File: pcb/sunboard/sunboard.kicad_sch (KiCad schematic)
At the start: 155 parts, among them SW1 SW_Push, SW10 SW_Push, SW100 SW_Push, SW101 SW_Push, SW102 SW_Push, SW103 SW_Push, SW104 SW_Push, SW105 SW_Push, SW106 SW_Push, SW107 SW_Push, SW108 SW_Push, SW109 SW_Push, SW11 SW_Push, SW110 SW_Push, SW111 SW_Push, SW112 SW_Push, SW113 SW_Push, SW114 SW_Push, SW115 SW_Push, SW116 SW_Push, SW117 SW_Push, SW118 SW_Push, SW119 SW_Push, SW12 SW_Push, SW120 SW_Push, SW121 SW_Push, SW122 SW_Push, SW123 SW_Push, SW124 SW_Push, SW125 SW_Push, SW126 SW_Push, SW127 SW_Push, SW128 SW_Push, SW129 SW_Push, SW13 SW_Push, SW130 SW_Push, SW131 SW_Push, SW132 SW_Push, SW133 SW_Push, SW134 SW_Push, SW135 SW_Push, SW136 SW_Push, SW137 SW_Push, SW138 SW_Push, SW139 SW_Push, SW14 SW_Push, SW140 SW_Push, SW141 SW_Push, SW142 SW_Push, SW143 SW_Push, SW144 SW_Push, SW145 SW_Push, SW146 SW_Push, SW147 SW_Push, SW148 SW_Push, SW149 SW_Push, SW15 SW_Push, SW150 SW_Push, SW151 SW_Push, SW152 SW_Push, SW153 SW_Push, SW154 SW_Push, SW16 SW_Push, SW17 SW_Push, SW18 SW_Push, SW19 SW_Push, SW2 SW_Push, SW20 SW_Push, SW21 SW_Push, SW22 SW_Push, SW23 SW_Push, SW24 SW_Push, SW25 SW_Push, SW26 SW_Push, SW27 SW_Push, SW28 SW_Push, SW29 SW_Push, SW3 SW_Push, SW30 SW_Push, SW31 SW_Push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

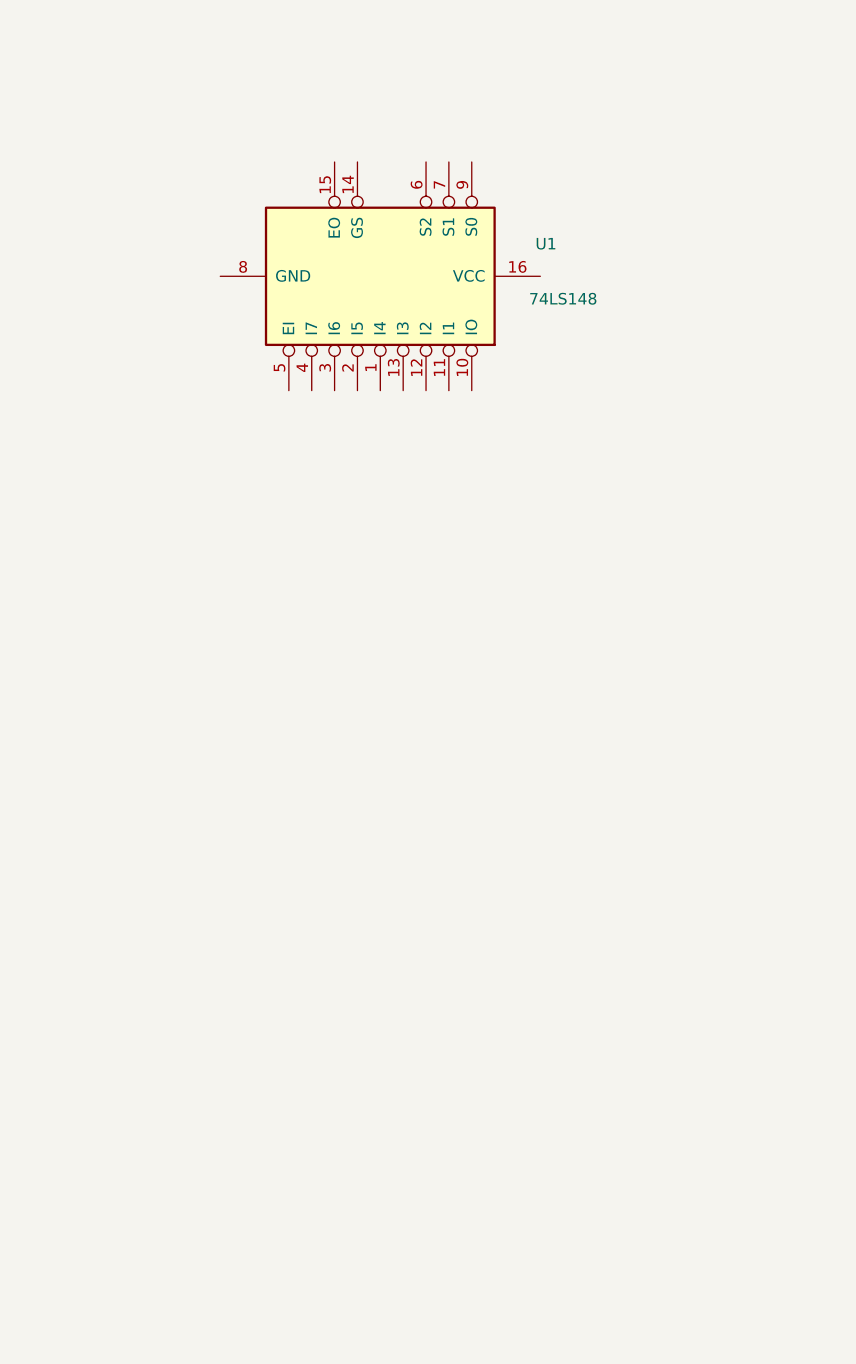
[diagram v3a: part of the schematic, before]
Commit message: feat(pcb): add 74hc4067 for mux/demux
Now the board uses 74hc4067 for both mux / demux purposes. A surprisingly nice chip with both functionalities. Might use it for the lights also
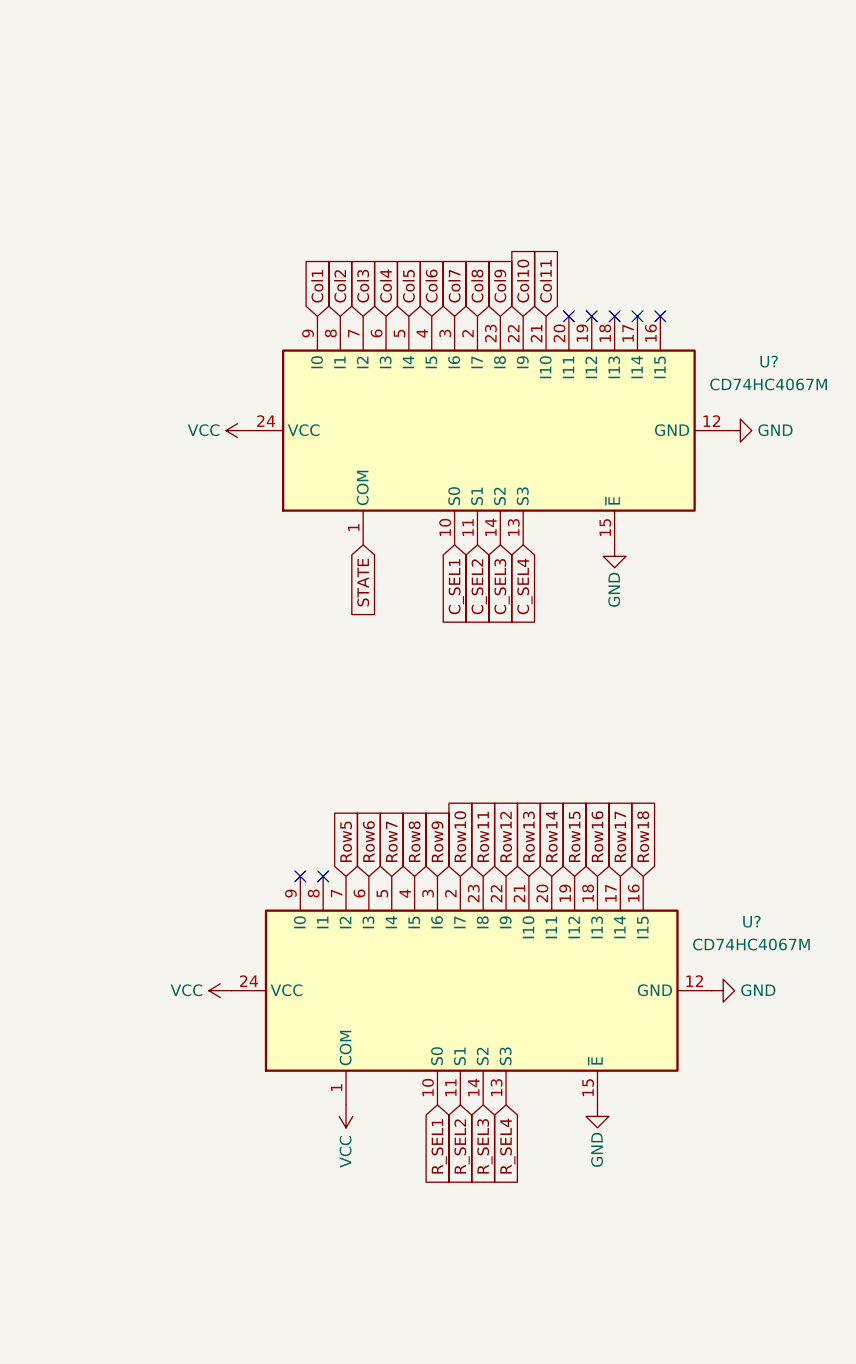
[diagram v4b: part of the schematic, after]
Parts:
- removed U1: 74LS148, symbol 74xx:74LS148
- added U? (x2): CD74HC4067M, Package_SO:SOIC-24W_7.5x15.4mm_P1.27mm, symbol 74xx:CD74HC4067M
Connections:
- net Col1: now also U?.9 (I0)
- net Col10: now also U?.22 (I9)
- net Col11: now also U?.21 (I10)
- net Col2: now also U?.8 (I1)
- net Col3: now also U?.7 (I2)
- net Col4: now also U?.6 (I3)
- net Col5: now also U?.5 (I4)
- net Col6: now also U?.4 (I5)
- net Col7: now also U?.3 (I6)
- net Col8: now also U?.2 (I7)
- net Col9: now also U?.23 (I8)
- net Row10: now also U?.2 (I7)
- net Row11: now also U?.23 (I8)
- net Row12: now also U?.22 (I9)
- net Row13: now also U?.21 (I10)
- net Row14: now also U?.20 (I11)
- net Row15: now also U?.19 (I12)
- net Row16: now also U?.18 (I13)
- net Row17: now also U?.17 (I14)
- net Row18: now also U?.16 (I15)
- net Row5: now also U?.7 (I2)
- net Row6: now also U?.6 (I3)
- net Row7: now also U?.5 (I4)
- net Row8: now also U?.4 (I5)
- net Row9: now also U?.3 (I6)
- new net C_SEL1: U?.10 (S0)
- new net C_SEL2: U?.11 (S1)
- new net C_SEL3: U?.14 (S2)
- new net C_SEL4: U?.13 (S3)
- new net GND: U?.12 (GND), U?.12 (GND), U?.15 (~{E}), U?.15 (~{E})
- new net R_SEL1: U?.10 (S0)
- new net R_SEL2: U?.11 (S1)
- new net R_SEL3: U?.14 (S2)
- new net R_SEL4: U?.13 (S3)
- new net STATE: U?.1 (COM)
- new net VCC: U?.1 (COM), U?.24 (VCC), U?.24 (VCC)
- no-connect marks 0 -> 7

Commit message: feat(pcb): migrate to subsheets
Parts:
- removed SW1, SW10, SW100, SW101, SW102, SW103, SW104, SW105, SW106, SW107, SW108, SW109, SW11, SW110, SW111, SW112, SW113, SW114, SW115, SW116, SW117, SW118, SW119, SW12, SW120, SW121, SW122, SW123, SW124, SW125, SW126, SW127, SW128, SW129, SW13, SW130, SW131, SW132, SW133, SW134, SW135, SW136, SW137, SW138, SW139, SW14, SW140, SW141, SW142, SW143, SW144, SW145, SW146, SW147, SW148, SW149, SW15, SW150, SW151, SW152, SW153, SW154, SW16, SW17, SW18, SW19, SW2, SW20, SW21, SW22, SW23, SW24, SW25, SW26, SW27, SW28, SW29, SW3, SW30, SW31, SW32, SW33, SW34, SW35, SW36, SW37, SW38, SW39, SW4, SW40, SW41, SW42, SW43, SW44, SW45, SW46, SW47, SW48, SW49, SW5, SW50, SW51, SW52, SW53, SW54, SW55, SW56, SW57, SW58, SW59, SW6, SW60, SW61, SW62, SW63, SW64, SW65, SW66, SW67, SW68, SW69, SW7, SW70, SW71, SW72, SW73, SW74, SW75, SW76, SW77, SW78, SW79, SW8, SW80, SW81, SW82, SW83, SW84, SW85, SW86, SW87, SW88, SW89, SW9, SW90, SW91, SW92, SW93, SW94, SW95, SW96, SW97, SW98, SW99: SW_Push, symbol Switch:SW_Push
- added U3: ESP32_NODEMCU, ESP32_NODEMCU:MODULE_ESP32_NODEMCU, symbol ESP32_NODEMCU:ESP32_NODEMCU
- gave numbers to parts that had none: 2
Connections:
- net GND: now also U3.J4_1 (GND_J4_1), U3.J4_7 (GND_J4_7), U3.J5_6 (GND_J5_6)
- net VCC: now also U3.J5_1 (5V)
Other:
- added sheet Button_Matrix (Button_Matrix.kicad_sch)
- added sheet LED_Matrix (LED_Matrix.kicad_sch)
- moved on the sheet: U1, U2

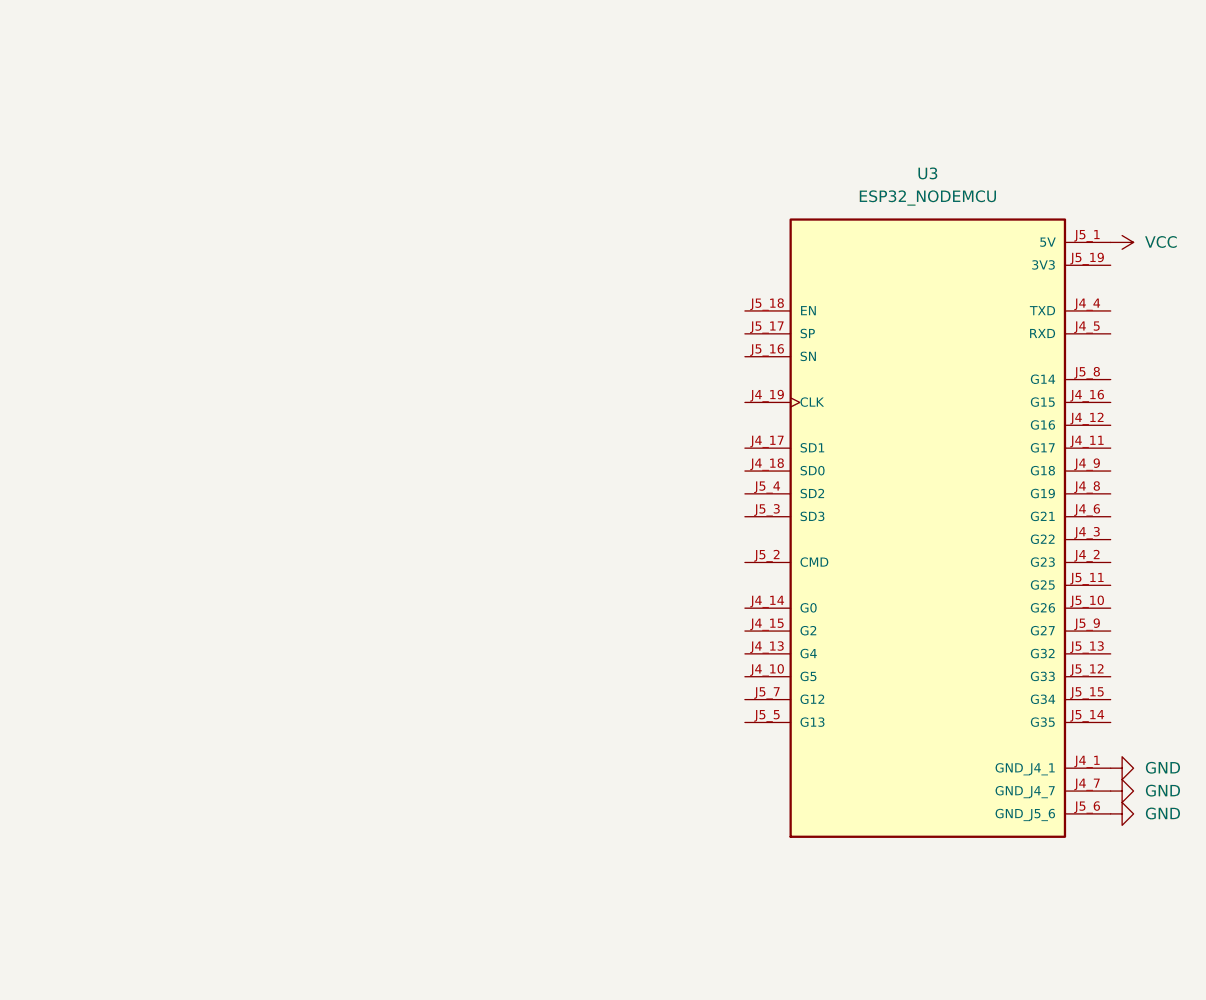
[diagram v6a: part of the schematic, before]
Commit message: feat(pcb): remove led driver, layout main grid
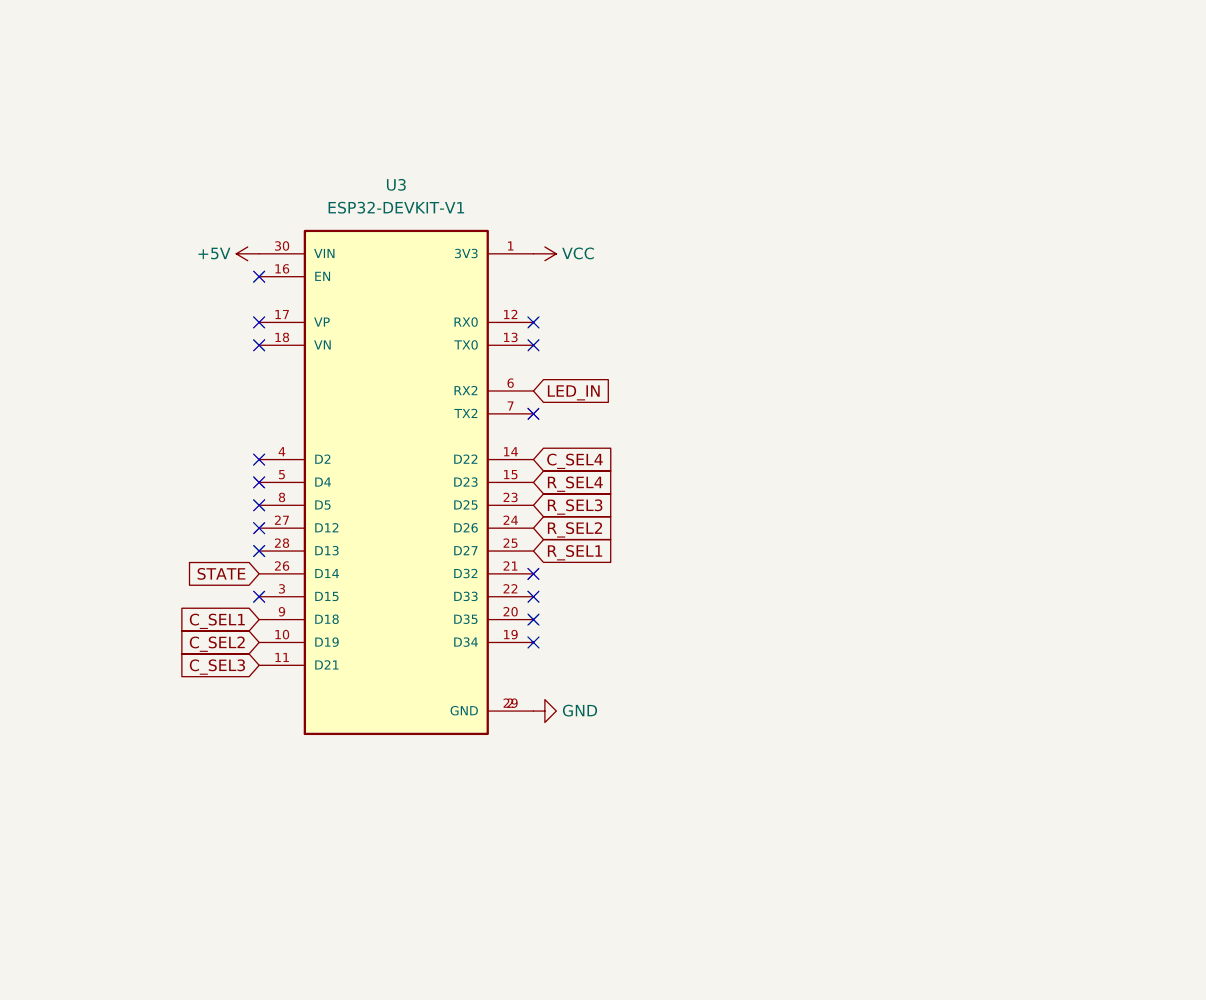
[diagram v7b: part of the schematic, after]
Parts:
- removed U3: ESP32_NODEMCU, ESP32_NODEMCU:MODULE_ESP32_NODEMCU, symbol ESP32_NODEMCU:ESP32_NODEMCU
- added U3: ESP32-DEVKIT-V1, ESP32-DEVKIT-V1:MODULE_ESP32_DEVKIT_V1, symbol ESP32-DEVKIT-V1:ESP32-DEVKIT-V1
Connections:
- net C_SEL1: now also U3.9 (D18)
- net C_SEL2: now also U3.10 (D19)
- net C_SEL3: now also U3.11 (D21)
- net C_SEL4: now also U3.14 (D22)
- net GND: now also U3.2 (GND), U3.29 (GND)
- net R_SEL1: now also U3.25 (D27)
- net R_SEL2: now also U3.24 (D26)
- net R_SEL3: now also U3.23 (D25)
- net R_SEL4: now also U3.15 (D23)
- net STATE: now also U3.26 (D14)
- net VCC: now also U3.1 (3V3)
- new net +5V: U3.30 (VIN)
- new net LED_IN: U3.6 (RX2)
- no-connect marks 7 -> 23

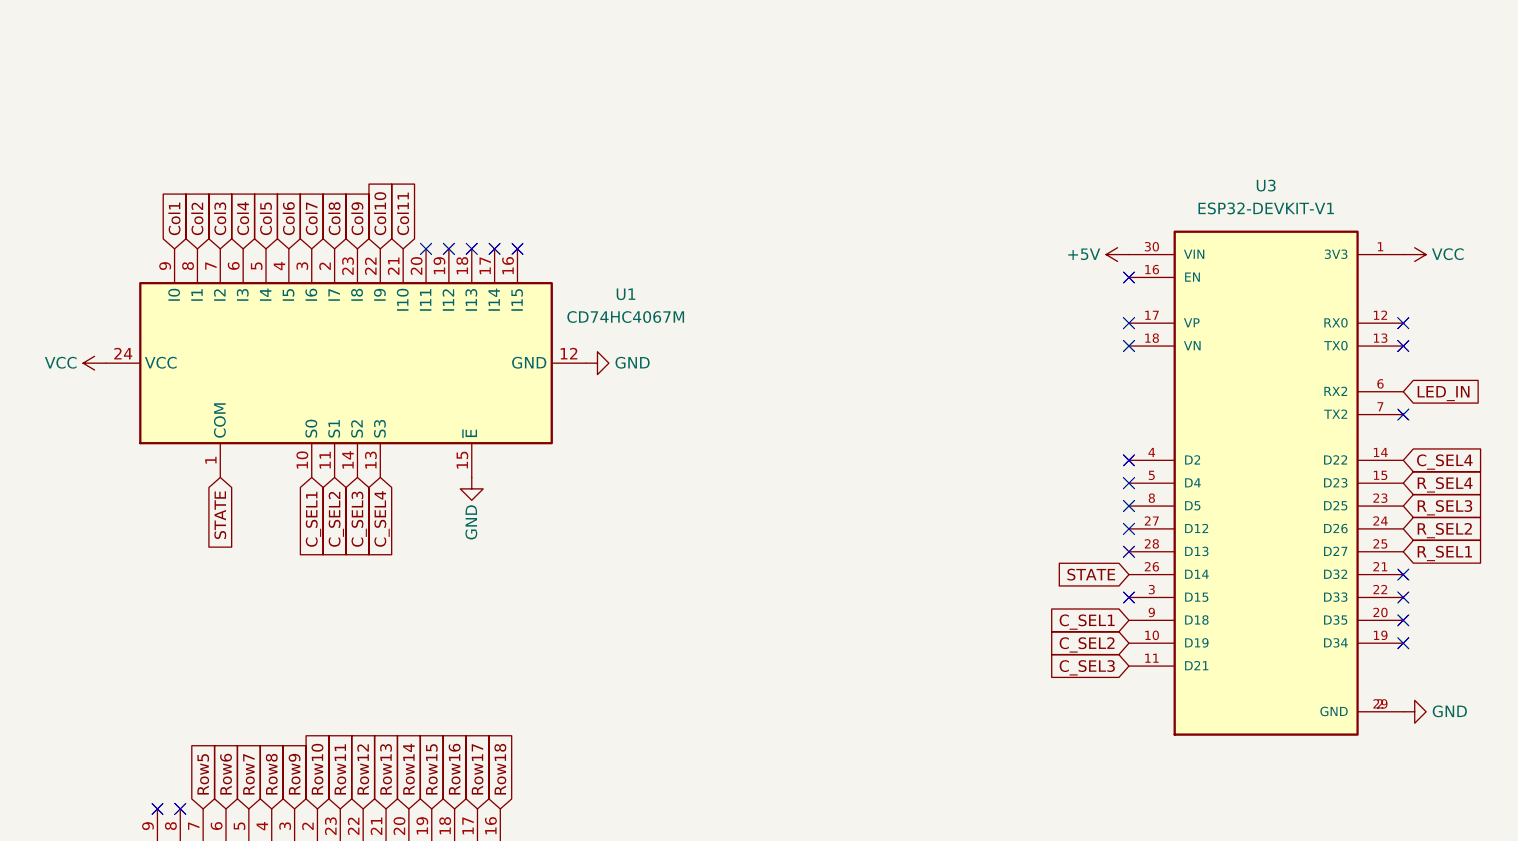
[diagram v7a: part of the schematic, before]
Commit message: feat(pcb): finish routing pcb
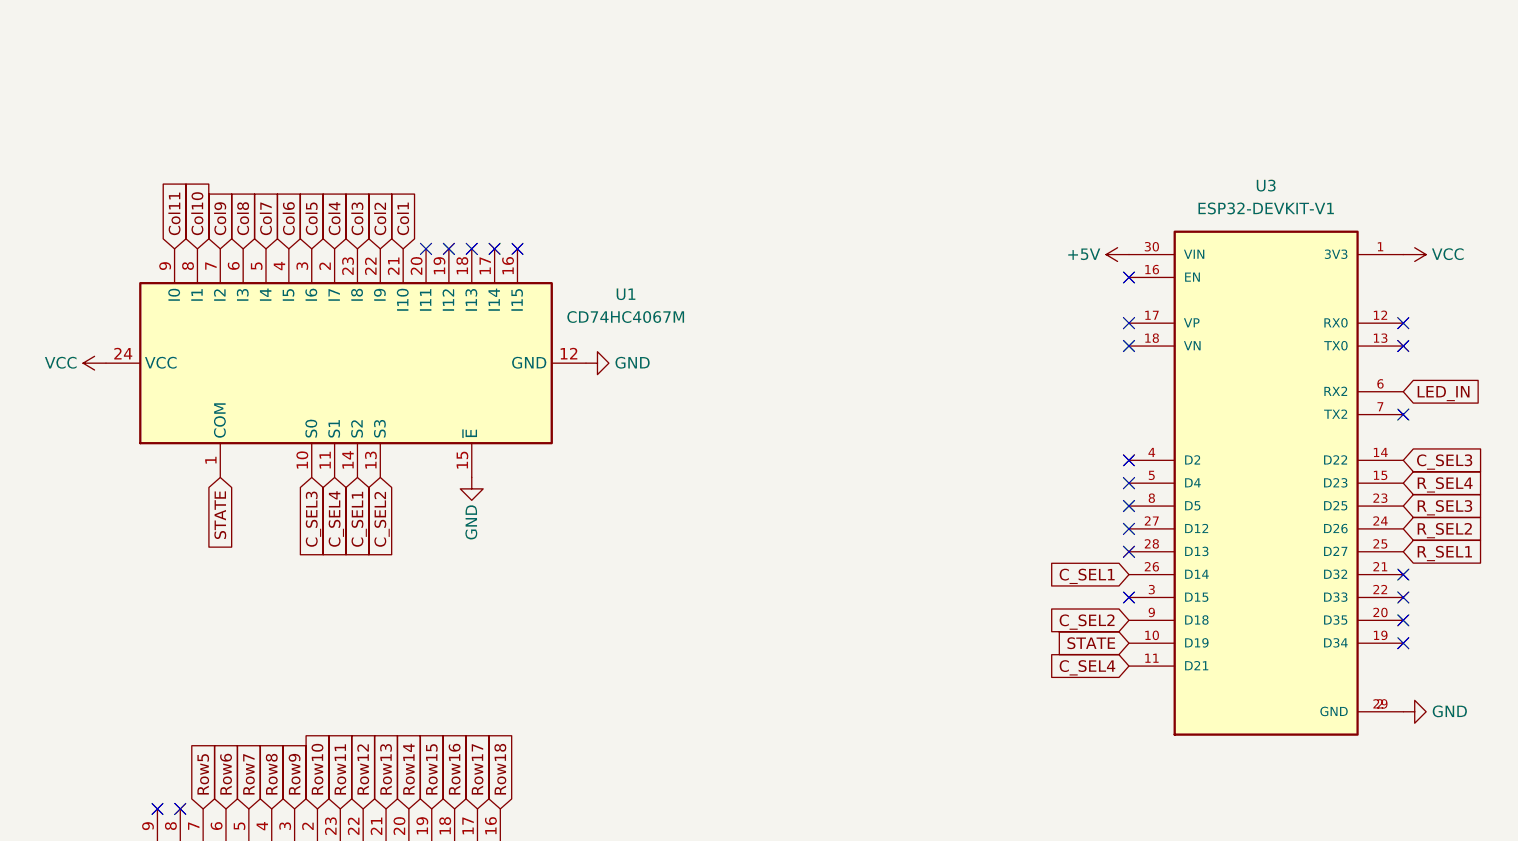
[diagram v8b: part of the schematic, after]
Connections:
- net C_SEL1: now also U1.14 (S2), U3.26 (D14); no longer U1.10 (S0), U3.9 (D18)
- net C_SEL2: now also U1.13 (S3), U3.9 (D18); no longer U1.11 (S1), U3.10 (D19)
- net C_SEL3: now also U1.10 (S0), U3.14 (D22); no longer U1.14 (S2), U3.11 (D21)
- net C_SEL4: now also U1.11 (S1), U3.11 (D21); no longer U1.13 (S3), U3.14 (D22)
- net Col1: now also U1.21 (I10); no longer U1.9 (I0)
- net Col10: now also U1.8 (I1); no longer U1.22 (I9)
- net Col11: now also U1.9 (I0); no longer U1.21 (I10)
- net Col2: now also U1.22 (I9); no longer U1.8 (I1)
- net Col3: now also U1.23 (I8); no longer U1.7 (I2)
- net Col4: now also U1.2 (I7); no longer U1.6 (I3)
- net Col5: now also U1.3 (I6); no longer U1.5 (I4)
- net Col7: now also U1.5 (I4); no longer U1.3 (I6)
- net Col8: now also U1.6 (I3); no longer U1.2 (I7)
- net Col9: now also U1.7 (I2); no longer U1.23 (I8)
- net STATE: now also U3.10 (D19); no longer U3.26 (D14)
